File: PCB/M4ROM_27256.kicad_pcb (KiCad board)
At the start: 2 copper layers, 38 x 16.6 mm, 7 parts, among them J1 32Kx8_mask_rom_socket, J2 4ROM_prog, SW1 CUS-14TB, U1 29F010

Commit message: pcb polish
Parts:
- J2: value 4ROM_prog -> 4ROM_prog_female
- SW1: footprint 000_LOCAL:SW_SP4T_CUS-14B -> 000_LOCAL:SW_SP4T_CUS-14B - PTH
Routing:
- net /A1: track 14.6 -> 10.8 mm, vias 1 -> 0
- net /~{OE}: track 17.0 -> 19.0 mm, vias 0 -> 1
- net /D1: track 12.4 -> 10.9 mm
- net /D5: track 12.3 -> 13.6 mm
- net /D3: track 16.6 -> 17.5 mm
- net /D0: track 10.7 -> 11.6 mm
- net /D4: track 15.6 -> 14.8 mm
- net /D2: track 12.7 -> 12.0 mm
- net GND: vias 39 -> 31

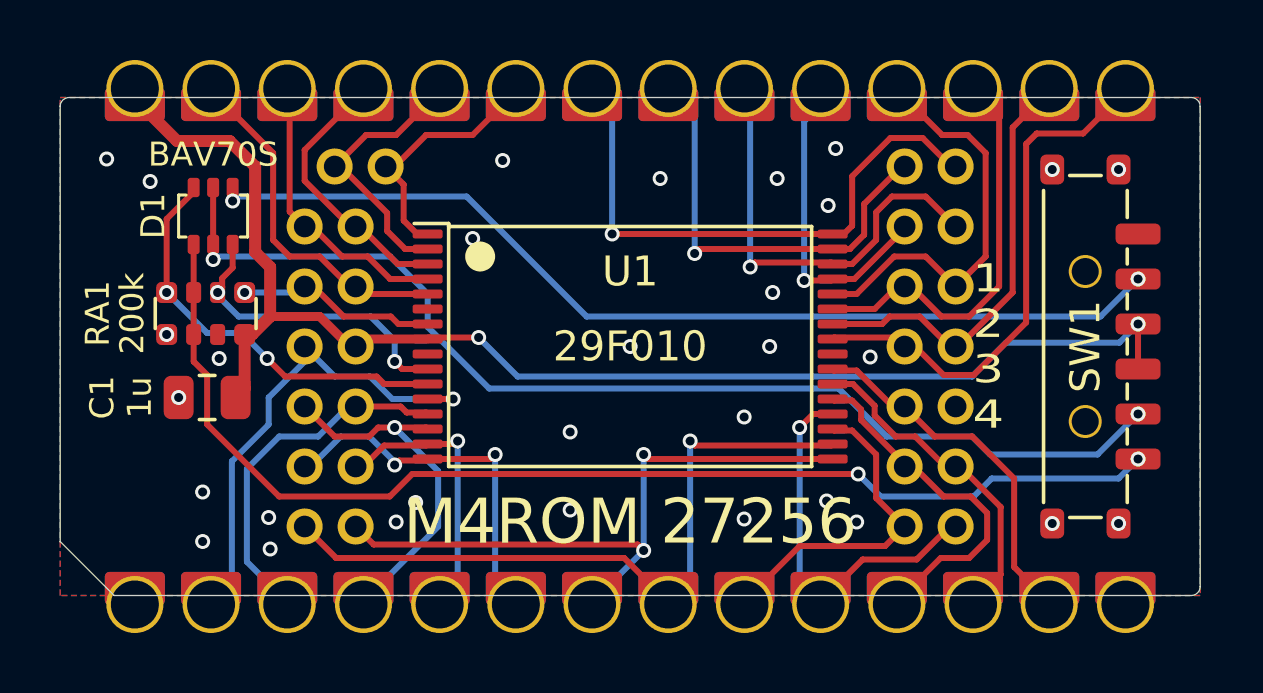
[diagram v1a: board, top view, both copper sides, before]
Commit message: improve some teardrops
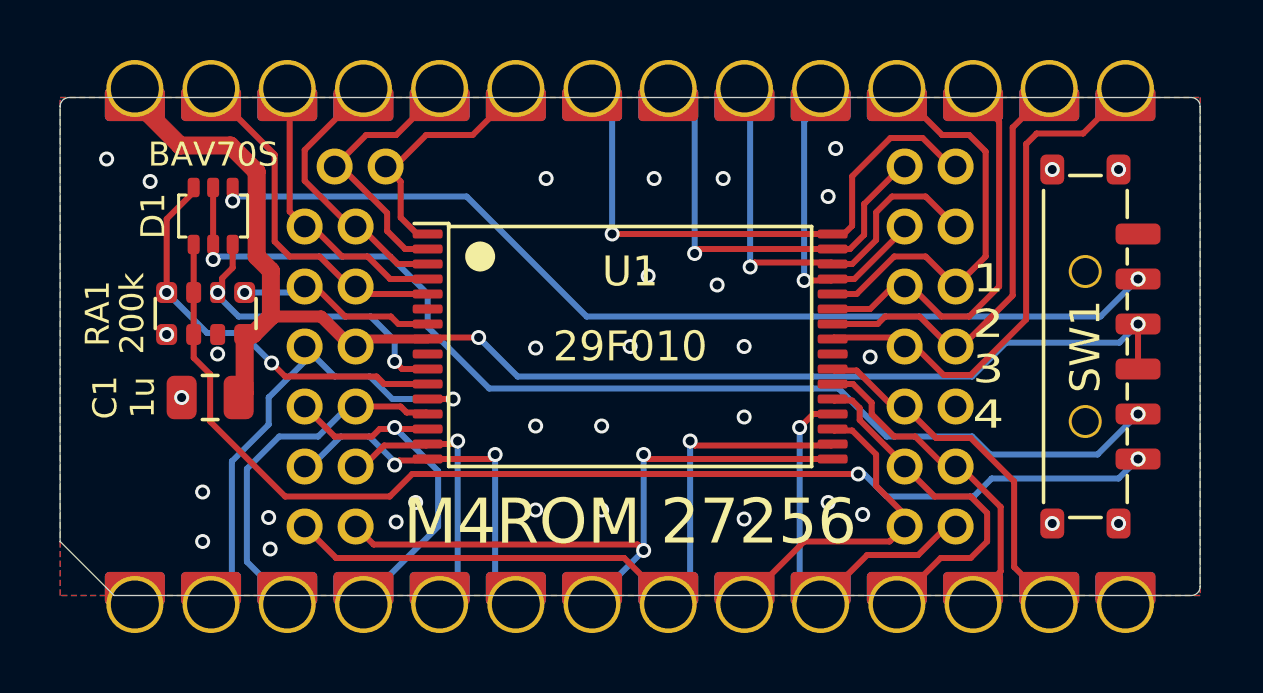
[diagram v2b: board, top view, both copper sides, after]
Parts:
- moved C1 0.10 mm to (133.2, 100.9)
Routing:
- net GND: vias 31 -> 34
